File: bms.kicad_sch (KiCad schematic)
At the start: 96 parts, among them J1 CELL_TAPS, J2 I2C_IN, J5 SWD, SW1 SW_Push, U1 LMR516xx, U2 STM32F103C8Tx, U3 ADuM1252, U4 MAX14920, U5 MAX11163, U6 MAX6126, Y1 8M

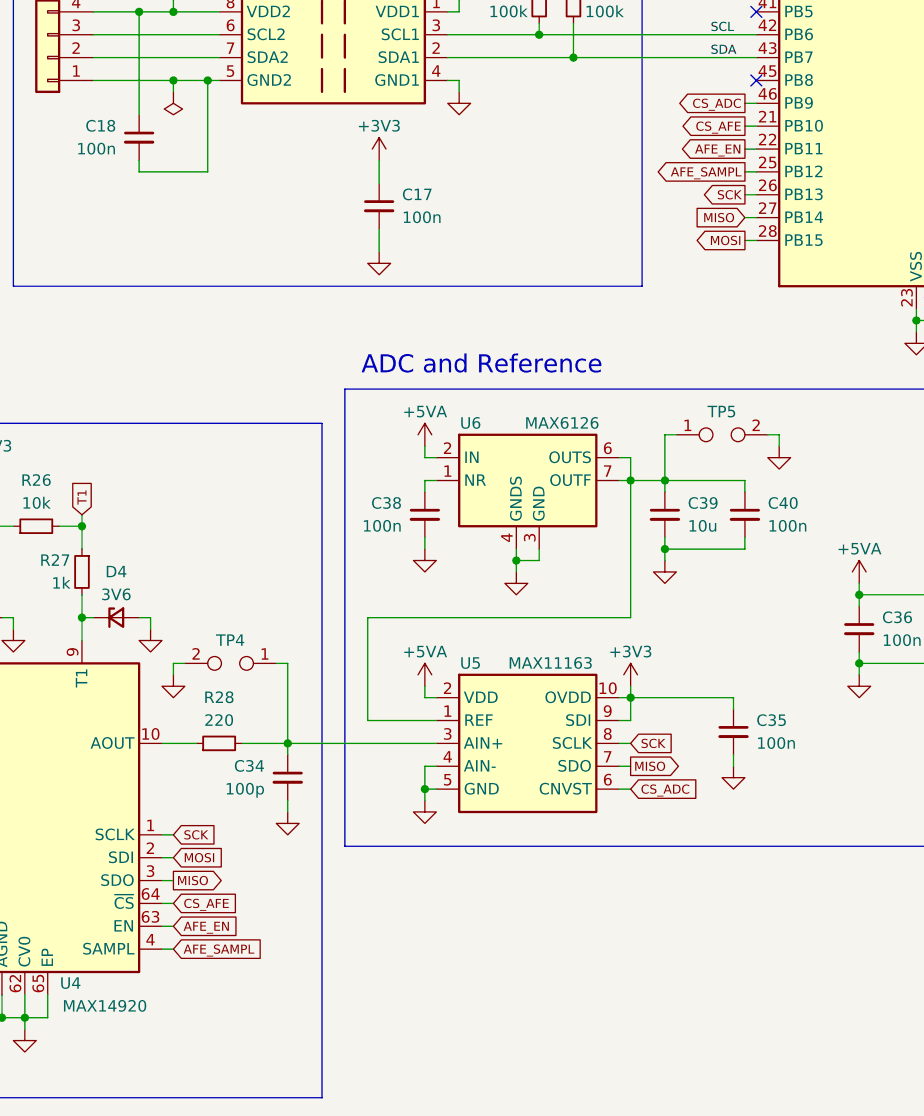
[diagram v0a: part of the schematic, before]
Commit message: *: Tie AFE SAMPL pin always high
Closes GH-2
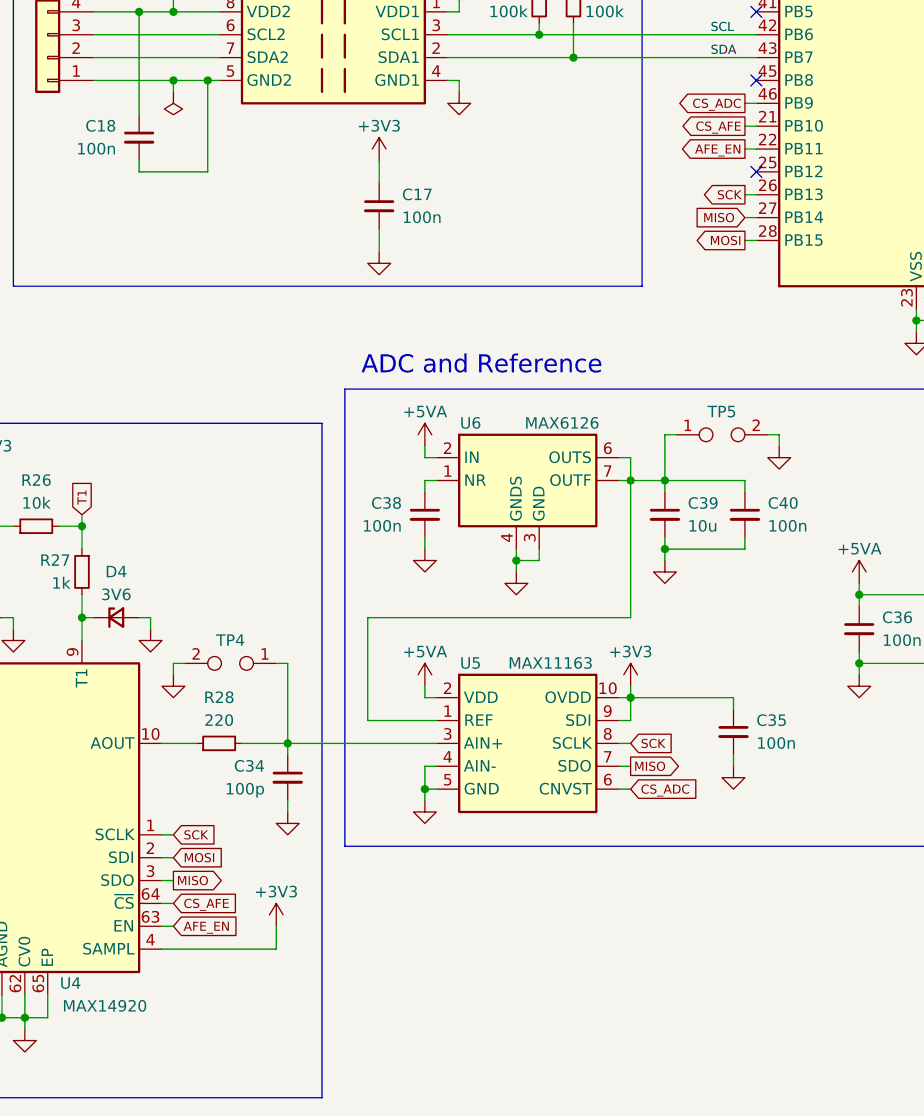
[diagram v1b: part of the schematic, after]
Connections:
- net +3V3: now also U4.4 (SAMPL)
- net AFE_SAMPL: no longer names the net of U2.25 (PB12)
- net AFE_SAMPL: no longer U4.4 (SAMPL)
- no-connect marks 14 -> 15
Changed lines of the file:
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@@
 	)
 	(no_connect
+		(at 214.63 88.9)
+	)
+	(no_connect
 		(at 214.63 63.5)
 	)
@@
 	(wire
 		(pts
+			(xy 161.29 175.26) (xy 148.59 175.26)
+		)
+		(stroke
+			(width 0)
+			(type default)
+		)
+	)
+	(wire
+		(pts
 			(xy 63.5 81.28) (xy 66.04 81.28)
 		)
@@
 	(wire
 		(pts
-			(xy 213.36 88.9) (xy 214.63 88.9)
-		)
-		(stroke
-			(width 0)
-			(type default)
-		)
-	)
-	(wire
-		(pts
 			(xy 57.15 53.34) (xy 57.15 54.61)
 		)
@@
 	(wire
 		(pts
+			(xy 161.29 172.72) (xy 161.29 175.26)
+		)
+		(stroke
+			(width 0)
+			(type default)
+		)
+	)
+	(wire
+		(pts
 			(xy 49.53 33.02) (xy 49.53 34.29)
 		)
@@
 	(wire
 		(pts
-			(xy 148.59 175.26) (xy 149.86 175.26)
-		)
-		(stroke
-			(width 0)
-			(type default)
-		)
-	)
-	(wire
-		(pts
 			(xy 179.07 31.75) (xy 187.96 31.75)
 		)
@@
 		)
 	)
-	(global_label "AFE_SAMPL"
-		(shape input)
-		(at 149.86 175.26 0)
-		(fields_autoplaced yes)
-		(effects
-			(font
-				(size 1 1)
-			)
-			(justify left)
-		)
-		(property "Intersheetrefs" "${INTERSHEET_REFS}"
-			(at 160.3531 175.26 0)
-			(effects
-				(font
-					(size 1.27 1.27)
-				)
-				(justify left)
-				(hide yes)
-			)
-		)
-	)
 	(global_label "TAP6"
 		(shape output)
@@
 		)
 	)
-	(global_label "AFE_SAMPL"
-		(shape output)
-		(at 213.36 88.9 180)
-		(fields_autoplaced yes)
-		(effects
-			(font
-				(size 1 1)
-			)
-			(justify right)
-		)
-		(property "Intersheetrefs" "${INTERSHEET_REFS}"
-			(at 202.8669 88.9 0)
-			(effects
-				(font
-					(size 1.27 1.27)
-				)
-				(justify right)
-				(hide yes)
-			)
-		)
-	)
 	(global_label "BA9"
 		(shape output)
@@
 					(unit 1)
 				)
+			)
+		)
+	)
+	(symbol
+		(lib_id "power:+3V3")
+		(at 161.29 172.72 0)
+		(unit 1)
+		(exclude_from_sim no)
+		(in_bom yes)
+		(on_board yes)
+		(dnp no)
+		(property "Reference" "#PWR063"
+			(at 161.29 176.53 0)
+			(effects
+				(font
+					(size 1.27 1.27)
+				)
+				(hide yes)
+			)
+		)
+		(property "Value" "+3V3"
+			(at 161.29 168.91 0)
+			(effects
+				(font
+					(size 1.27 1.27)
+				)
+			)
+		)
+		(property "Footprint" ""
+			(at 161.29 172.72 0)
+			(effects
+				(font
+					(size 1.27 1.27)
+				)
+				(hide yes)
+			)
+		)
+		(property "Datasheet" ""
+			(at 161.29 172.72 0)
+			(effects
+				(font
+					(size 1.27 1.27)
+				)
+				(hide yes)
+			)
+		)
+		(property "Description" "Power symbol creates a global label with name \"+3V3\""
+			(at 161.29 172.72 0)
+			(effects
+				(font
+					(size 1.27 1.27)
+				)
+				(hide yes)
+			)
+		)
+		(pin "1"
+		)
+		(instances
+			(project "bms"
+				(path "/ae4a7653-8e6d-4e05-b144-1e5e3b2092b7"
+					(reference "#PWR063")
+					(unit 1)
+				)

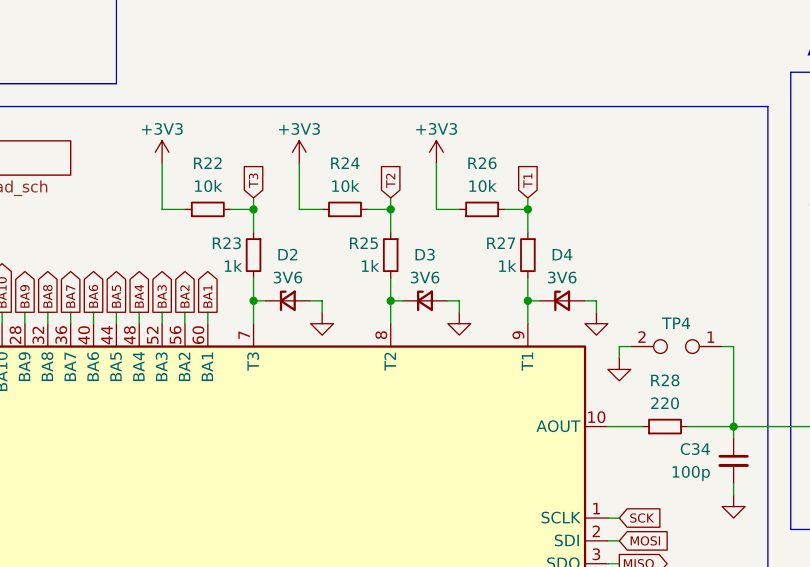
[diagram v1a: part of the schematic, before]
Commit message: *: Remove thermistor protection zener diodes
Closes GH-8
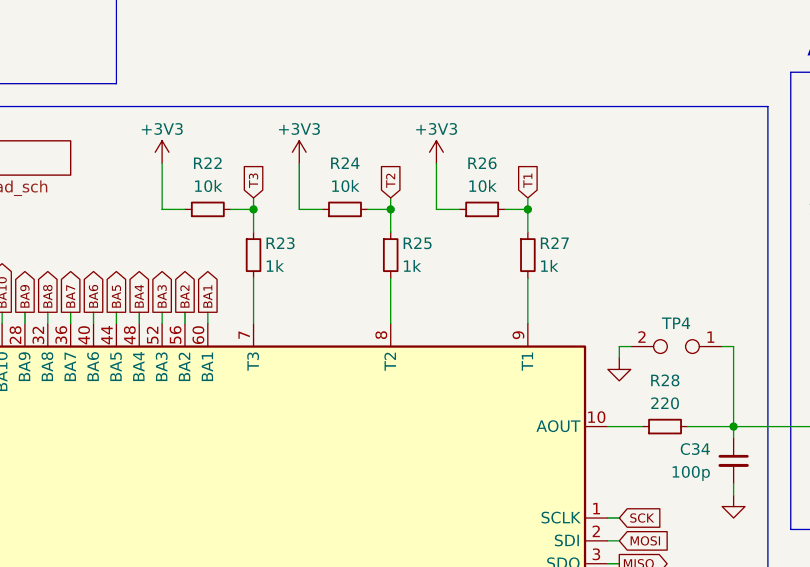
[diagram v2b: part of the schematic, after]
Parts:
- removed D2, D3, D4: 3V6, Diode_SMD:D_SOD-323, symbol Device:D_Zener_Small

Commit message: *: Fix whitespace in BOM
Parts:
- F1: Dist # C2153714 -> C2153714
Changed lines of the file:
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@@
 			)
 		)
-		(property "Dist #" " C2153714"
+		(property "Dist #" "C2153714"
 			(at 69.85 74.93 0)
 			(effects

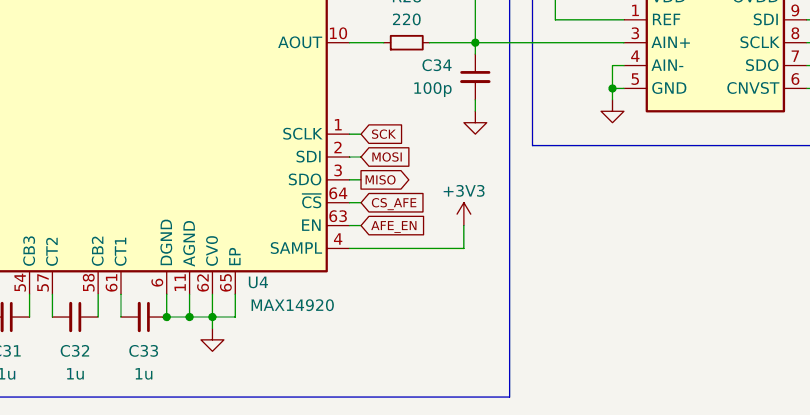
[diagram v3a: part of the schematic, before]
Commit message: *: Add a pull-down on the MAX14920 enable pin
Closes GH-13
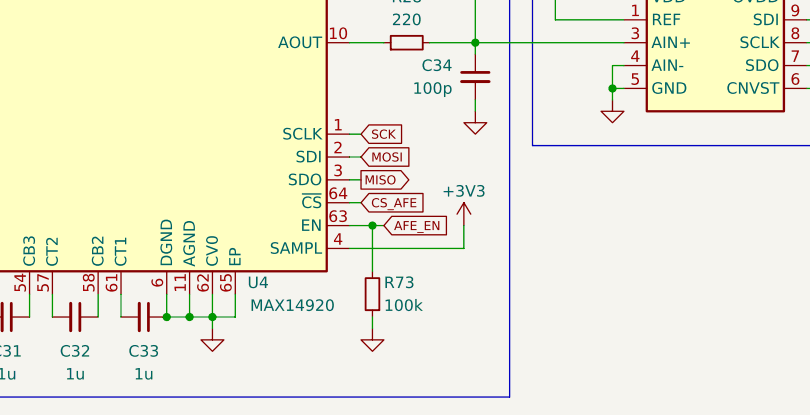
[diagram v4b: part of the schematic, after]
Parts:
- added R73: 100k, Resistor_SMD:R_0603_1608Metric, symbol Device:R_Small
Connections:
- net AFE_EN: now also R73.2
- net GND: now also R73.1
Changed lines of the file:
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@@
 	)
 	(junction
+		(at 151.13 172.72)
+		(diameter 0)
+		(color 0 0 0 0)
+	)
+	(junction
 		(at 177.8 157.48)
 		(diameter 0)
@@
 	(wire
 		(pts
-			(xy 148.59 172.72) (xy 149.86 172.72)
+			(xy 148.59 172.72) (xy 151.13 172.72)
 		)
 		(stroke
@@
 	(wire
 		(pts
+			(xy 151.13 182.88) (xy 151.13 184.15)
+		)
+		(stroke
+			(width 0)
+			(type default)
+		)
+	)
+	(wire
+		(pts
 			(xy 250.19 38.1) (xy 254 38.1)
 		)
@@
 	(wire
 		(pts
+			(xy 151.13 172.72) (xy 151.13 177.8)
+		)
+		(stroke
+			(width 0)
+			(type default)
+		)
+	)
+	(wire
+		(pts
 			(xy 46.99 40.64) (xy 46.99 39.37)
 		)
@@
 	(wire
 		(pts
+			(xy 151.13 172.72) (xy 152.4 172.72)
+		)
+		(stroke
+			(width 0)
+			(type default)
+		)
+	)
+	(wire
+		(pts
 			(xy 212.09 147.32) (xy 200.66 147.32)
 		)
@@
 	(global_label "AFE_EN"
 		(shape input)
-		(at 149.86 172.72 0)
+		(at 152.4 172.72 0)
 		(fields_autoplaced yes)
 		(effects
@@
 		)
 		(property "Intersheetrefs" "${INTERSHEET_REFS}"
-			(at 157.5436 172.72 0)
+			(at 160.0836 172.72 0)
 			(effects
 				(font
@@
 	)
 	(symbol
+		(lib_id "Device:R_Small")
+		(at 151.13 180.34 180)
+		(unit 1)
+		(exclude_from_sim no)
+		(in_bom yes)
+		(on_board yes)
+		(dnp no)
+		(property "Reference" "R73"
+			(at 152.4 179.07 0)
+			(effects
+				(font
+					(size 1.27 1.27)
+				)
+				(justify right)
+			)
+		)
+		(property "Value" "100k"
+			(at 152.4 181.61 0)
+			(effects
+				(font
+					(size 1.27 1.27)
+				)
+				(justify right)
+			)
+		)
+		(property "Footprint" "Resistor_SMD:R_0603_1608Metric"
+			(at 151.13 180.34 0)
+			(effects
+				(font
+					(size 1.27 1.27)
+				)
+				(hide yes)
+			)
+		)
+		(property "Datasheet" "~"
+			(at 151.13 180.34 0)
+			(effects
+				(font
+					(size 1.27 1.27)
+				)
+				(hide yes)
+			)
+		)
+		(property "Description" "Resistor, small symbol"
+			(at 151.13 180.34 0)
+			(effects
+				(font
+					(size 1.27 1.27)
+				)
+				(hide yes)
+			)
+		)
+		(property "Dist #" "C25803"
+			(at 151.13 180.34 0)
+			(effects
+				(font
+					(size 1.27 1.27)
+				)
+				(hide yes)
+			)
+		)
+		(property "Mfr" "Uni-Royal"
+			(at 151.13 180.34 0)
+			(effects
+				(font
+					(size 1.27 1.27)
+				)
+				(hide yes)
+			)
+		)
+		(property "Mfr #" "0603WAF1003T5E"
+			(at 151.13 180.34 0)
+			(effects
+				(font
+					(size 1.27 1.27)
+				)
+				(hide yes)
+			)
+		)
+		(property "Dist" "LCSC"
+			(at 151.13 180.34 0)
+			(effects
+				(font
+					(size 1.27 1.27)
+				)
+				(hide yes)
+			)
+		)
+		(pin "1"
+		)
+		(pin "2"
+		)
+		(instances
+			(project "bms"
+				(path "/ae4a7653-8e6d-4e05-b144-1e5e3b2092b7"
+					(reference "R73")
+					(unit 1)
+				)
+			)
+		)
+	)
+	(symbol
 		(lib_id "Device:C_Small")
 		(at 179.07 27.94 0)
@@
 					(unit 1)
 				)
+			)
+		)
+	)
+	(symbol
+		(lib_id "power:GND")
+		(at 151.13 184.15 0)
+		(unit 1)
+		(exclude_from_sim no)
+		(in_bom yes)
+		(on_board yes)
+		(dnp no)
+		(fields_autoplaced yes)
+		(property "Reference" "#PWR027"
+			(at 151.13 190.5 0)
+			(effects
+				(font
+					(size 1.27 1.27)
+				)
+				(hide yes)
+			)
+		)
+		(property "Value" "GND"
+			(at 151.13 189.23 0)
+			(effects
+				(font
+					(size 1.27 1.27)
+				)
+				(hide yes)
+			)
+		)
+		(property "Footprint" ""
+			(at 151.13 184.15 0)
+			(effects
+				(font
+					(size 1.27 1.27)
+				)
+				(hide yes)
+			)
+		)
+		(property "Datasheet" ""
+			(at 151.13 184.15 0)
+			(effects
+				(font
+					(size 1.27 1.27)
+				)
+				(hide yes)
+			)
+		)
+		(property "Description" "Power symbol creates a global label with name \"GND\" , ground"
+			(at 151.13 184.15 0)
+			(effects
+				(font
+					(size 1.27 1.27)
+				)
+				(hide yes)
+			)
+		)
+		(pin "1"
+		)
+		(instances
+			(project "bms"
+				(path "/ae4a7653-8e6d-4e05-b144-1e5e3b2092b7"
+					(reference "#PWR027")
+					(unit 1)
+				)

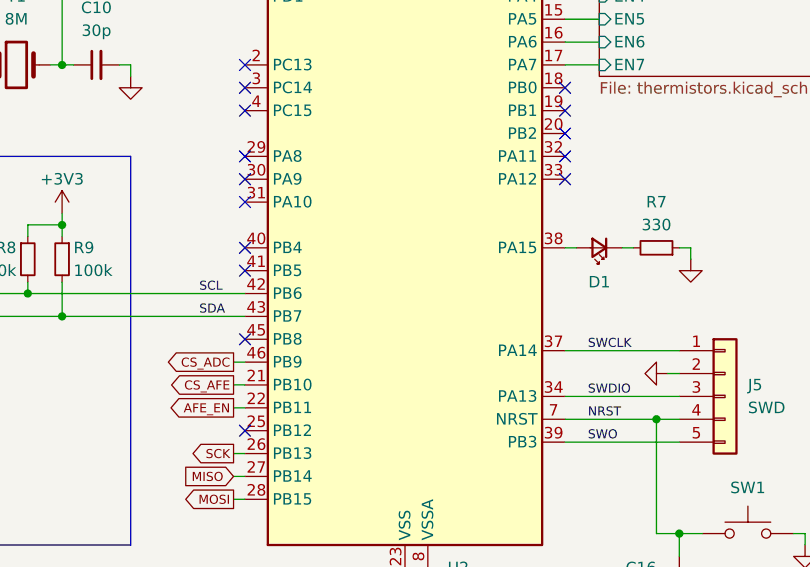
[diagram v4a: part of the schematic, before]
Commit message: *: Change MCU LED pin
Closes GH-3
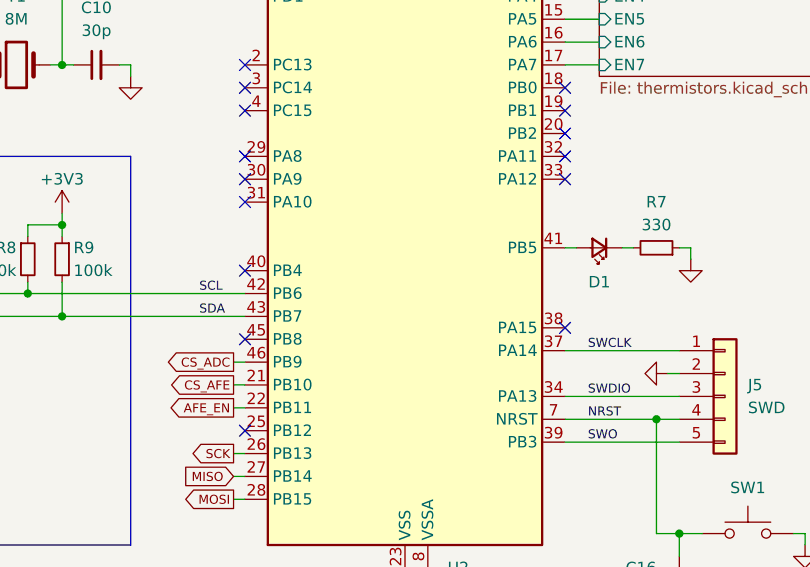
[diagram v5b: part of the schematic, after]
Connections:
- net at U2.38 (PA15): no longer D1.2 (A)
- net at U2.41 (PB5): now also D1.2 (A)
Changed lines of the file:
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@@
+	)
+	(no_connect
+		(at 250.19 77.47)
 	)
 	(no_connect
@@
 	)
 	(no_connect
-		(at 214.63 68.58)
-	)
-	(no_connect

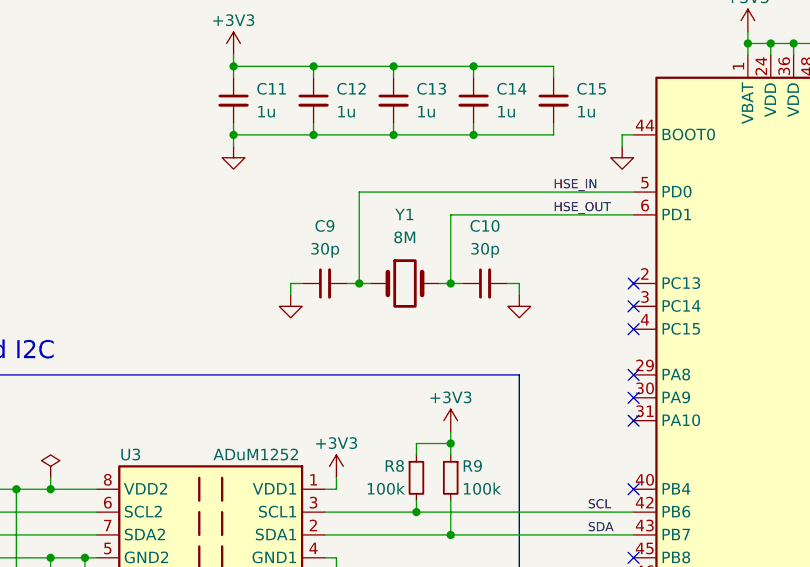
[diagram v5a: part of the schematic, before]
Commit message: *: Mark MCU crystal as DNP
Closes GH-6
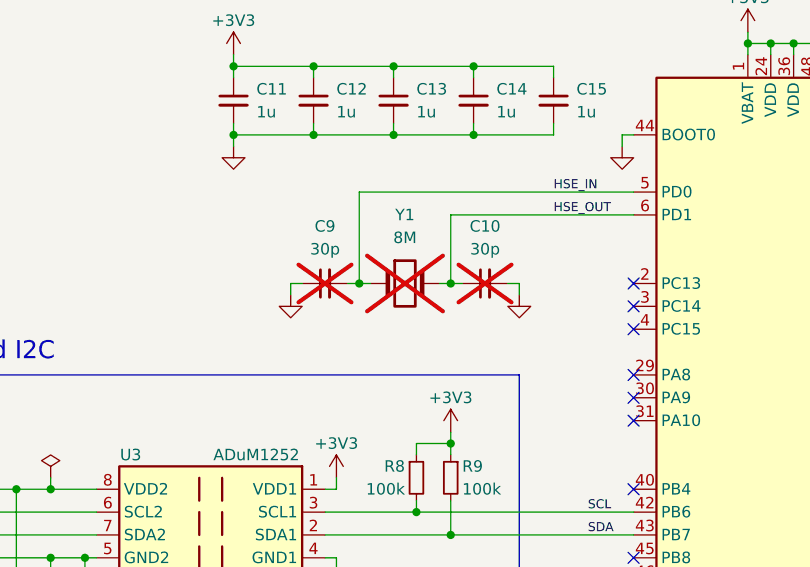
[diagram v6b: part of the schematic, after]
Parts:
- C10, C9, Y1: now not fitted
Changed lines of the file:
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@@
 		(in_bom yes)
 		(on_board yes)
-		(dnp no)
+		(dnp yes)
 		(fields_autoplaced yes)
 		(property "Reference" "C9"
@@
 		(in_bom yes)
 		(on_board yes)
-		(dnp no)
+		(dnp yes)
 		(fields_autoplaced yes)
 		(property "Reference" "C10"
@@
 		(in_bom yes)
 		(on_board yes)
-		(dnp no)
+		(dnp yes)
 		(property "Reference" "Y1"
 			(at 189.23 40.64 0)

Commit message: *: Use a more suitable footprint for the MAX14920
This one has a more correct exposed pad size. Closes GH-4
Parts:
- U4: footprint Package_QFP:TQFP-64-1EP_10x10mm_P0.5mm_EP8x8mm -> Package_QFP:TQFP-64-1EP_10x10mm_P0.5mm_EP5.305x5.305mm
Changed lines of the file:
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@@
 			)
 		)
-		(property "Footprint" "Package_QFP:TQFP-64-1EP_10x10mm_P0.5mm_EP8x8mm"
+		(property "Footprint" "Package_QFP:TQFP-64-1EP_10x10mm_P0.5mm_EP5.305x5.305mm"
 			(at 89.154 166.878 90)
 			(effects

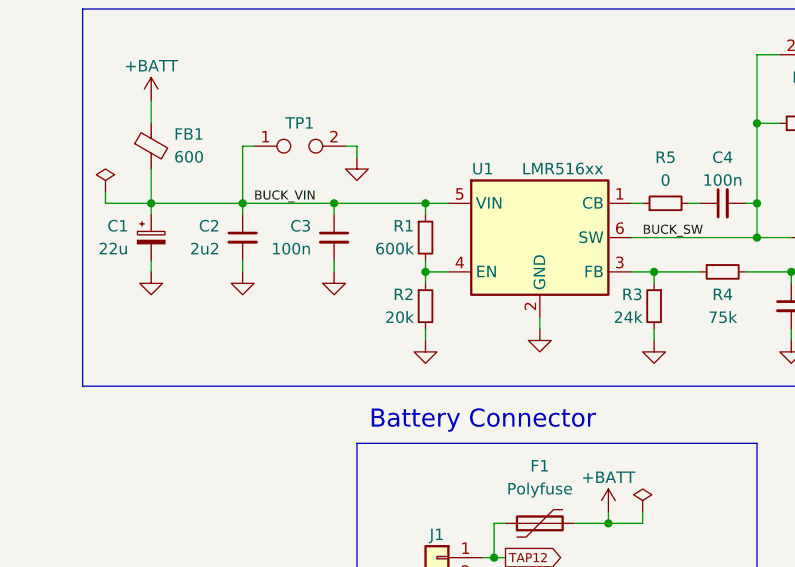
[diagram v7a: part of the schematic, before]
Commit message: *: Change buck enable pin potential divider values
Closes GH-12
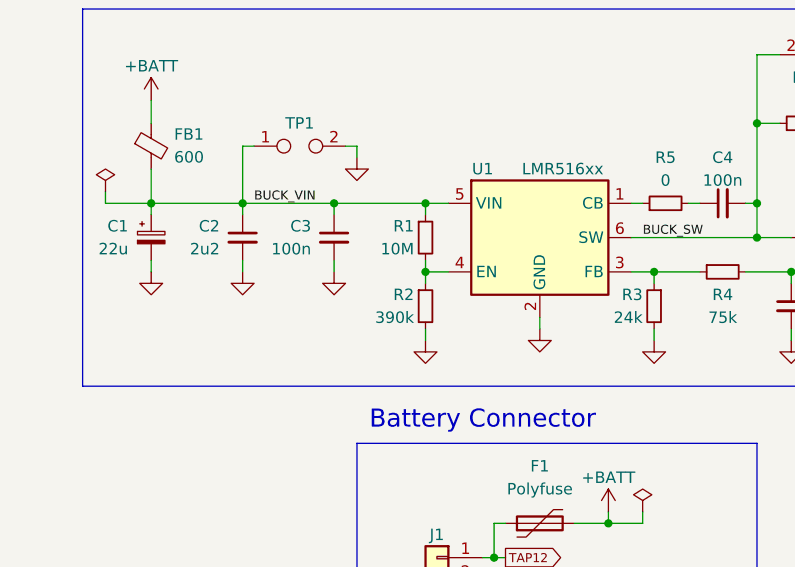
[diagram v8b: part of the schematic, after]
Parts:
- R1: value 600k -> 10M
- R2: value 20k -> 390k
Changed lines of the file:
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@@
 			)
 		)
-		(property "Value" "20k"
+		(property "Value" "390k"
 			(at 55.88 52.07 0)
 			(effects
@@
 			)
 		)
-		(property "Value" "600k"
+		(property "Value" "10M"
 			(at 55.88 44.45 0)
 			(effects
